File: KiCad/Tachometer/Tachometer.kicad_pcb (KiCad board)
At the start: 2 copper layers, 105 parts, among them J1 PJ301M-12, J2 PJ301M-12, J3 PJ301M-12, J4 PJ301M-12, J5 PJ301M-12, J6 PJ301M-12, J7 PJ301M-12, J8 PJ301M-12, J9 PJ301M-12, Q1 2N3904, Q10 2N3904, Q11 2N3904, Q12 2N3904, Q13 2N3904, Q14 2N3904, Q15 2N3904, Q16 2N3904, Q17 2N3904, Q18 2N3904, Q2 2N3904, Q3 2N3904, Q4 2N3904, Q5 2N3904, Q6 2N3904, Q7 2N3904, Q8 2N3904, Q9 2N3904

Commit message: all work
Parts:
- C1, C2, C3: value CP1_Small -> 470n; moved to B.Cu
- C10, C11, C12, C13, C14, C15, C5, C6, C7, C8, C9: value CP1_Small -> 100n; moved to B.Cu
- C16, C17, C18: value CP1_Small -> 22u; moved to B.Cu
- C4, H1, Q1, Q10, Q11, Q12, Q13, Q14, Q15, Q16, Q17, Q18, Q2, Q3, Q4, Q5, Q6, Q7, Q8, Q9, R1, R10, R11, R12, R13, R14, R15, R16, R17, R18, R19, R2, R20, R21, R22, R23, R24, R25, R26, R27, R28, R29, R3, R30, R31, R32, R33, R34, R35, R36, R37, R38, R39, R4, R40, R41, R42, R43, R44, R45, R5, R6, R7, R8, R9: moved to B.Cu
- D10, D11, D12: value 1N4006 -> LED; footprint Diode_THT:D_A-405_P12.70mm_Horizontal -> LED_THT:LED_D3.0mm_FlatTop
- D3, D4, D5: value LED -> 1N4006; footprint LED_THT:LED_D3.0mm_FlatTop -> Diode_THT:D_A-405_P12.70mm_Horizontal; moved to B.Cu
- moved H1 262.7 mm to (53.3, 189.2), turned to 90 degrees
- moved D3 232.2 mm to (47.0, 161.3), turned to 270 degrees
- moved D5 224.3 mm to (34.3, 161.3), turned to 270 degrees
- moved D4 187.6 mm to (59.7, 174.0), turned to 90 degrees
- moved A1 167.5 mm to (80.0, 110.5), turned to 180 degrees
- moved J3 167.5 mm to (111.8, 48.3), turned to 0 degrees
- moved D11 164.5 mm to (167.6, 20.3)
- moved D10 164.2 mm to (175.3, 29.2)
- moved J9 163.9 mm to (137.2, 39.4), turned to 0 degrees
- moved D12 156.2 mm to (175.3, 20.3)
- moved Q2 156.1 mm to (80.0, 152.4)
- moved J8 154.6 mm to (148.6, 21.6), turned to 0 degrees
- moved R23 151.4 mm to (203.2, 170.2)
- moved J5 150.5 mm to (125.7, 39.4), turned to 0 degrees
- moved Q1 148.3 mm to (80.0, 146.1), turned to 0 degrees
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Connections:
- A1 pad 30: +12V -> 12V
- C1 pad 1: GND -> 5V
- C1 pad 2: -12V -> GND
- C10 pad 1: GND -> 5V
- C10 pad 2: -12V -> GND
- C11 pad 1: +12V -> 12V
- C12 pad 1: +5V -> GND
- C12 pad 2: GND -> -12V
- C13 pad 1: GND -> 5V
- C13 pad 2: -12V -> GND
- C14 pad 1: +12V -> 12V
- C15 pad 1: +5V -> GND
- C15 pad 2: GND -> -12V
- C16 pad 1: GND -> 5V
- C16 pad 2: -12V -> GND
- C17 pad 1: +12V -> 12V
- C18 pad 1: +5V -> GND
- C18 pad 2: GND -> -12V
- C2 pad 1: +12V -> 12V
- C3 pad 1: +5V -> GND
- C3 pad 2: GND -> -12V
- C4 pad 1: GND -> 5V
- C4 pad 2: -12V -> GND
- C5 pad 1: +12V -> 12V
- C6 pad 1: +5V -> GND
- C6 pad 2: GND -> -12V
- C7 pad 1: GND -> 5V
- C7 pad 2: -12V -> GND
- C8 pad 1: +12V -> 12V
- C9 pad 1: +5V -> GND
- C9 pad 2: GND -> -12V
- D10 pad 1: +5V -> GND
- D11 pad 1: Net-(D11-Pad1) -> GND
- D11 pad 2: -12V -> Net-(D11-Pad2)
- D12 pad 1: +12V -> GND
- D3 pad 1: GND -> 12V
- D4 pad 1: GND -> Net-(D4-Pad1)
- D4 pad 2: Net-(D4-Pad2) -> -12V
- D5 pad 1: GND -> 5V
- H1 pad 1: Net-(FB2-Pad1) -> Net-(D4-Pad1)
- H1 pad 10: Net-(FB3-Pad1) -> Net-(D3-Pad2)
- H1 pad 11: Net-(FB1-Pad1) -> Net-(D5-Pad2)
- H1 pad 12: Net-(FB1-Pad1) -> Net-(D5-Pad2)
- H1 pad 2: Net-(FB2-Pad1) -> Net-(D4-Pad1)
- H1 pad 9: Net-(FB3-Pad1) -> Net-(D3-Pad2)
- Q11 pad 3: Net-(Q11-Pad3) -> Net-(J6-Pad3)
- Q14 pad 3: Net-(J8-Pad3) -> Net-(Q14-Pad3)
- Q15 pad 3: Net-(J9-Pad3) -> Net-(J8-Pad3)
- Q17 pad 3: Net-(Q17-Pad3) -> Net-(J9-Pad3)
- Q2 pad 3: Net-(J2-Pad3) -> Net-(Q2-Pad3)
- Q3 pad 3: Net-(J3-Pad3) -> Net-(J2-Pad3)
- Q4 pad 3: Net-(J4-Pad3) -> Net-(Q4-Pad3)
- Q5 pad 3: Net-(J5-Pad3) -> Net-(J3-Pad3)
- Q6 pad 3: Net-(J6-Pad3) -> Net-(Q6-Pad3)
- Q7 pad 3: Net-(Q7-Pad3) -> Net-(J4-Pad3)
- Q9 pad 3: Net-(Q9-Pad3) -> Net-(J5-Pad3)
- R1 pad 1: Net-(Q7-Pad3) -> 5V
- R1 pad 2: Net-(Q1-Pad2) -> Net-(J1-Pad3)
- R10 pad 1: +5V -> Net-(D2-Pad2)
- R10 pad 2: Net-(J4-Pad3) -> Net-(Q4-Pad2)
- R11 pad 1: +5V -> 5V
- R11 pad 2: Net-(J5-Pad3) -> Net-(J3-Pad3)
- R12 pad 1: +5V -> Net-(Q6-Pad3)
- R12 pad 2: Net-(J6-Pad3) -> Net-(Q5-Pad2)
- R13 pad 1: Net-(D1-Pad2) -> 5V
- R13 pad 2: Net-(Q7-Pad2) -> Net-(Q6-Pad3)
- R14 pad 1: Net-(D2-Pad2) -> Tr3
- R14 pad 2: Net-(Q8-Pad2) -> Net-(Q6-Pad2)
- R15 pad 1: Net-(D3-Pad2) -> Net-(D6-Pad2)
- R15 pad 2: Net-(Q9-Pad2) -> Net-(Q6-Pad2)
- R16 pad 1: Net-(D4-Pad2) -> 5V
- R16 pad 2: Net-(Q10-Pad2) -> Net-(J4-Pad3)
- R17 pad 1: Net-(D5-Pad2) -> Net-(Q8-Pad3)
- R17 pad 2: Net-(Q11-Pad2) -> Net-(Q7-Pad2)
- R18 pad 1: Net-(D6-Pad2) -> 5V
- R18 pad 2: Net-(Q12-Pad2) -> Net-(Q8-Pad3)
- R19 pad 1: +5V -> Tr4
- R19 pad 2: Net-(Q7-Pad3) -> Net-(Q8-Pad2)
- R2 pad 1: Net-(Q8-Pad3) -> Net-(Q2-Pad3)
- R2 pad 2: Net-(Q2-Pad2) -> Net-(Q1-Pad2)
- R20 pad 1: +5V -> Net-(D7-Pad2)
- R20 pad 2: Net-(Q8-Pad3) -> Net-(Q8-Pad2)
- R21 pad 1: +5V -> 5V
- R21 pad 2: Net-(Q9-Pad3) -> Net-(J5-Pad3)
- R22 pad 1: +5V -> Net-(Q10-Pad3)
- R22 pad 2: Net-(Q10-Pad3) -> Net-(Q9-Pad2)
- R23 pad 1: +5V -> 5V
- R23 pad 2: Net-(Q11-Pad3) -> Net-(Q10-Pad3)
- R24 pad 1: +5V -> Tr5
- R24 pad 2: Net-(Q12-Pad3) -> Net-(Q10-Pad2)
- R25 pad 1: Tr1 -> Net-(D8-Pad2)
- R25 pad 2: Net-(Q7-Pad2) -> Net-(Q10-Pad2)
- R26 pad 1: Tr2 -> 5V
- R26 pad 2: Net-(Q8-Pad2) -> Net-(J6-Pad3)
- R27 pad 1: Tr3 -> Net-(Q12-Pad3)
- R27 pad 2: Net-(Q9-Pad2) -> Net-(Q11-Pad2)
- R28 pad 1: Tr4 -> 5V
- R28 pad 2: Net-(Q10-Pad2) -> Net-(Q12-Pad3)
- R29 pad 1: Tr5 -> Tr6
- R29 pad 2: Net-(Q11-Pad2) -> Net-(Q12-Pad2)
- R3 pad 1: Net-(Q9-Pad3) -> 5V
- R3 pad 2: Net-(Q3-Pad2) -> Net-(Q2-Pad3)
- R30 pad 1: Tr6 -> Net-(D9-Pad2)
- R31 pad 1: Net-(Q16-Pad3) -> 5V
- R31 pad 2: Net-(Q13-Pad2) -> Net-(J7-Pad3)
- R32 pad 1: Net-(Q17-Pad3) -> Net-(Q14-Pad3)
- R32 pad 2: Net-(Q14-Pad2) -> Net-(Q13-Pad2)
- R33 pad 1: Net-(Q18-Pad3) -> 5V
- R33 pad 2: Net-(Q15-Pad2) -> Net-(Q14-Pad3)
- R34 pad 1: +5V -> Tr7
- R34 pad 2: Net-(J7-Pad3) -> Net-(Q14-Pad2)
- R35 pad 1: +5V -> Net-(D10-Pad2)
- R35 pad 2: Net-(J8-Pad3) -> Net-(Q14-Pad2)
- R36 pad 1: +5V -> 5V
- R36 pad 2: Net-(J9-Pad3) -> Net-(J8-Pad3)
- R37 pad 1: Net-(D7-Pad2) -> Net-(Q16-Pad3)
- R37 pad 2: Net-(Q16-Pad2) -> Net-(Q15-Pad2)
- R38 pad 1: Net-(D8-Pad2) -> 5V
- R38 pad 2: Net-(Q17-Pad2) -> Net-(Q16-Pad3)
- R39 pad 1: Net-(D9-Pad2) -> Tr8
- R39 pad 2: Net-(Q18-Pad2) -> Net-(Q16-Pad2)
- R4 pad 1: Net-(Q10-Pad3) -> Tr1
- R4 pad 2: Net-(Q4-Pad2) -> Net-(Q2-Pad2)
- R40 pad 1: +5V -> Net-(D11-Pad2)
- R40 pad 2: Net-(Q16-Pad3) -> Net-(Q16-Pad2)
- R41 pad 1: +5V -> 5V
- R41 pad 2: Net-(Q17-Pad3) -> Net-(J9-Pad3)
- R42 pad 1: +5V -> Net-(Q18-Pad3)
- R42 pad 2: Net-(Q18-Pad3) -> Net-(Q17-Pad2)
- R43 pad 1: Tr7 -> 5V
- R43 pad 2: Net-(Q16-Pad2) -> Net-(Q18-Pad3)
- R44 pad 1: Tr8 -> Tr9
- R44 pad 2: Net-(Q17-Pad2) -> Net-(Q18-Pad2)
- R45 pad 1: Tr9 -> Net-(D12-Pad2)
- R5 pad 1: Net-(Q11-Pad3) -> Net-(D1-Pad2)
- R5 pad 2: Net-(Q5-Pad2) -> Net-(Q2-Pad2)
- R6 pad 1: Net-(Q12-Pad3) -> 5V
- R6 pad 2: Net-(Q6-Pad2) -> Net-(J2-Pad3)
- R7 pad 1: +5V -> Net-(Q4-Pad3)
- R7 pad 2: Net-(J1-Pad3) -> Net-(Q3-Pad2)
- R8 pad 1: +5V -> 5V
- R8 pad 2: Net-(J2-Pad3) -> Net-(Q4-Pad3)
- R9 pad 1: +5V -> Tr2
- R9 pad 2: Net-(J3-Pad3) -> Net-(Q4-Pad2)

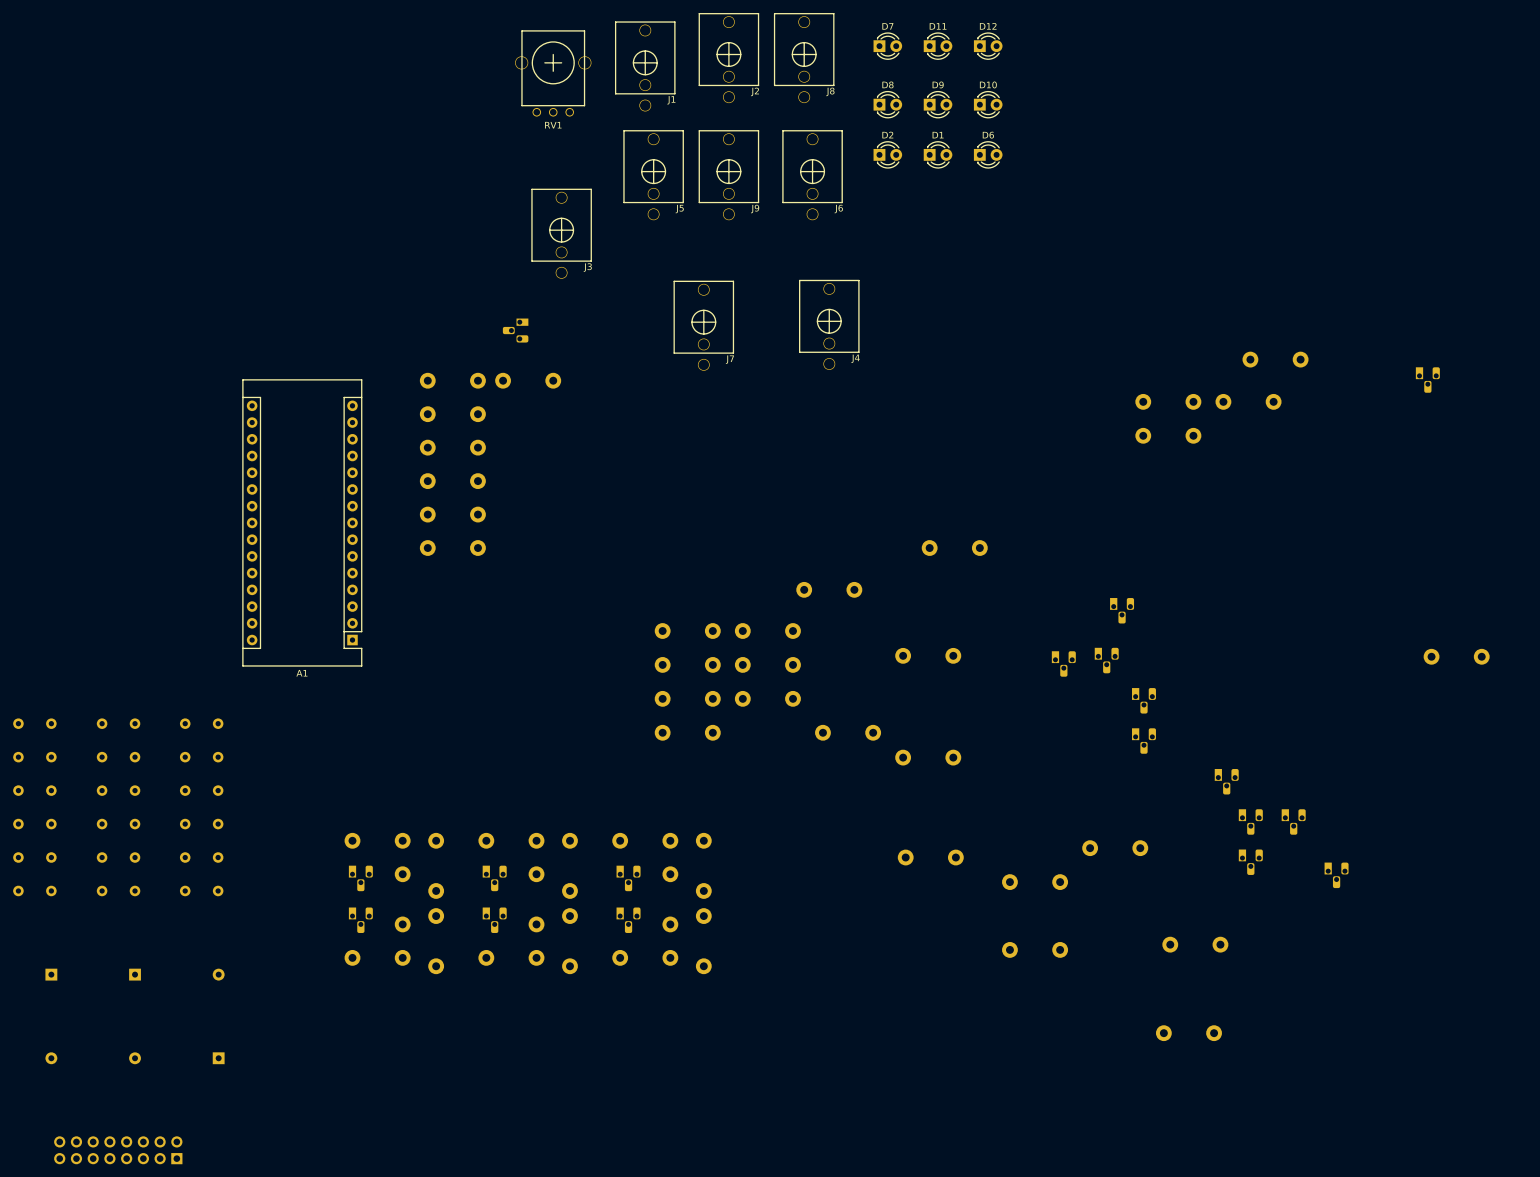
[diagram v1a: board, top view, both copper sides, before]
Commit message: added smd footprints
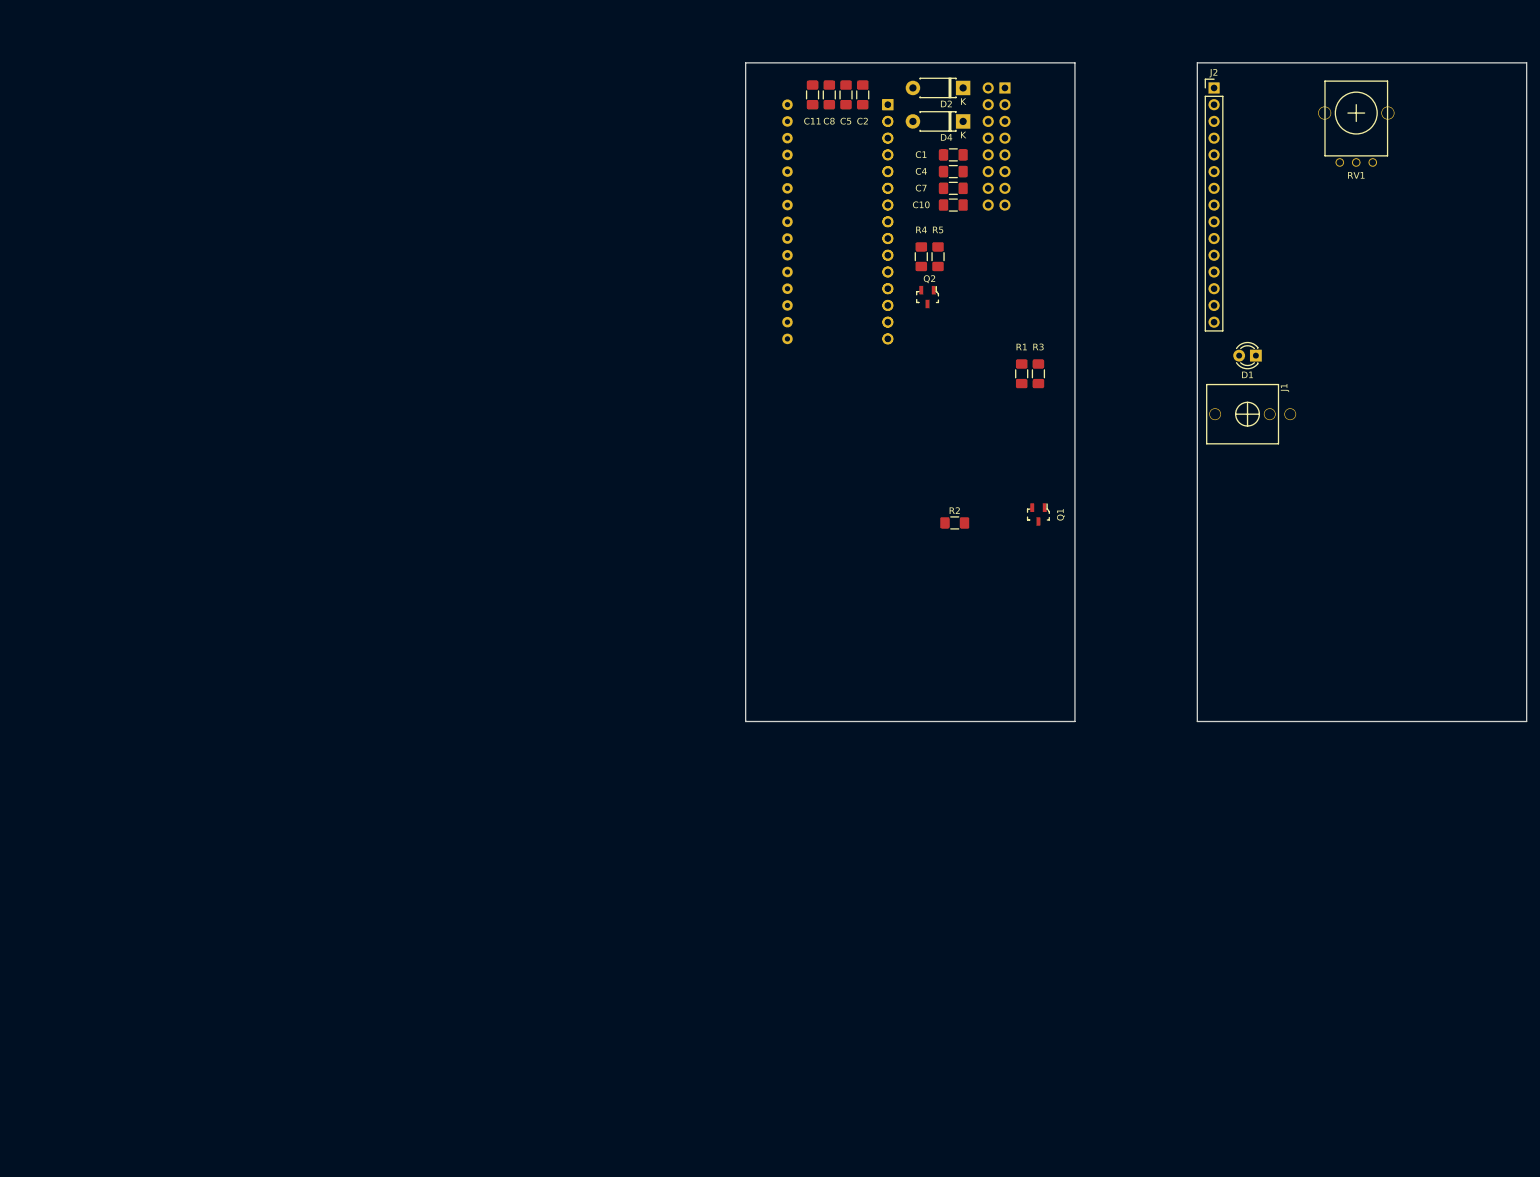
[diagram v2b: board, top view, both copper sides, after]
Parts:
- removed C12, C13, C14, C15, C6, C9: 100n, Capacitor_THT:C_Disc_D10.0mm_W2.5mm_P5.00mm
- removed C16, C17, C18: 22u, Capacitor_THT:C_Disc_D10.0mm_W2.5mm_P5.00mm
- removed C3: 470n, Capacitor_THT:C_Disc_D10.0mm_W2.5mm_P5.00mm
- removed D10, D11, D12, D6, D7, D8, D9: LED, LED_THT:LED_D3.0mm_FlatTop
- removed D3, D5: 1N4006, Diode_THT:D_A-405_P12.70mm_Horizontal
- removed J4, J5, J6, J7, J8, J9: PJ301M-12, eurorack:PJ301M-12
- removed Q10, Q11, Q12, Q13, Q14, Q15, Q16, Q17, Q18, Q3, Q4, Q5, Q6, Q7, Q8, Q9: 2N3904, Package_TO_SOT_THT:TO-92L_HandSolder
- removed R10, R11, R12, R13, R14, R15, R16, R17, R18, R19, R20, R21, R22, R23, R24, R25, R26, R27, R28, R29, R30, R31, R32, R33, R34, R35, R36, R37, R38, R39, R40, R41, R42, R43, R44, R45, R6, R7, R8, R9: R_US, Resistor_THT:R_Axial_DIN0411_L9.9mm_D3.6mm_P7.62mm_Vertical
- A1: moved to B.Cu
- C1, C2: footprint Capacitor_THT:C_Disc_D10.0mm_W2.5mm_P5.00mm -> Capacitor_SMD:C_1206_3216Metric_Pad1.42x1.75mm_HandSolder; moved to F.Cu
- C10, C11, C5, C7, C8: value 100n -> 470n; footprint Capacitor_THT:C_Disc_D10.0mm_W2.5mm_P5.00mm -> Capacitor_SMD:C_1206_3216Metric_Pad1.42x1.75mm_HandSolder; moved to F.Cu
- C4: value CP1_Small -> 470n; footprint Capacitor_THT:C_Disc_D10.0mm_W2.5mm_P5.00mm -> Capacitor_SMD:C_1206_3216Metric_Pad1.42x1.75mm_HandSolder; moved to F.Cu
- D2: value LED -> 1N4006; footprint LED_THT:LED_D3.0mm_FlatTop -> Diode_THT:D_DO-41_SOD81_P7.62mm_Horizontal
- D4: footprint Diode_THT:D_A-405_P12.70mm_Horizontal -> Diode_THT:D_DO-41_SOD81_P7.62mm_Horizontal; moved to F.Cu
- J2: value PJ301M-12 -> Conn_01x15_MountingPin; footprint eurorack:PJ301M-12 -> Connector_PinHeader_2.54mm:PinHeader_1x15_P2.54mm_Vertical
- J3: value PJ301M-12 -> Conn_01x15_MountingPin; footprint eurorack:PJ301M-12 -> Connector_PinHeader_2.54mm:PinHeader_1x15_P2.54mm_Vertical; moved to B.Cu
- Q1, Q2: footprint Package_TO_SOT_THT:TO-92L_HandSolder -> digikey-footprints:SOT-23-3; moved to F.Cu
- R1, R2, R4: value R_US -> 1k; footprint Resistor_THT:R_Axial_DIN0411_L9.9mm_D3.6mm_P7.62mm_Vertical -> Resistor_SMD:R_1206_3216Metric_Pad1.42x1.75mm_HandSolder; moved to F.Cu
- R3: value R_US -> 10k; footprint Resistor_THT:R_Axial_DIN0411_L9.9mm_D3.6mm_P7.62mm_Vertical -> Resistor_SMD:R_1206_3216Metric_Pad1.42x1.75mm_HandSolder; moved to F.Cu
- R5: value R_US -> 200; footprint Resistor_THT:R_Axial_DIN0411_L9.9mm_D3.6mm_P7.62mm_Vertical -> Resistor_SMD:R_1206_3216Metric_Pad1.42x1.75mm_HandSolder; moved to F.Cu
- moved H1 205.5 mm to (179.1, 26.7), turned to 180 degrees
- moved D4 181.7 mm to (172.7, 31.8), turned to 180 degrees
- moved C1 176.8 mm to (171.2, 36.8), turned to 0 degrees
- moved C10 169.0 mm to (171.2, 44.5), turned to 0 degrees
- moved C7 164.7 mm to (171.2, 41.9), turned to 0 degrees
- moved C2 163.8 mm to (157.5, 27.7), turned to 270 degrees
- moved C4 163.3 mm to (171.2, 39.4), turned to 0 degrees
- moved C11 154.9 mm to (149.9, 27.7), turned to 270 degrees
- moved C5 151.0 mm to (154.9, 27.7), turned to 270 degrees
- moved C8 145.7 mm to (152.4, 27.7), turned to 270 degrees
- moved R4 137.1 mm to (166.4, 52.3), turned to 270 degrees
- moved Q2 128.3 mm to (167.3, 58.4), turned to 270 degrees
- moved R5 125.8 mm to (168.9, 52.3)
- moved RV1 122.2 mm to (232.4, 30.5)
- moved R1 117.7 mm to (181.6, 70.1), turned to 270 degrees
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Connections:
- A1 pad 10: Tr6 -> Net-(A1-Pad10)
- A1 pad 11: Tr7 -> Net-(A1-Pad11)
- A1 pad 12: Tr8 -> Net-(A1-Pad12)
- A1 pad 13: Tr9 -> Net-(A1-Pad13)
- A1 pad 5: Tr1 -> Net-(A1-Pad5)
- A1 pad 6: Tr2 -> Net-(A1-Pad6)
- A1 pad 7: Tr3 -> Net-(A1-Pad7)
- A1 pad 8: Tr4 -> Net-(A1-Pad8)
- A1 pad 9: Tr5 -> Net-(A1-Pad9)
- D2 pad 1: GND -> Net-(D2-Pad1)
- D2 pad 2: Net-(D2-Pad2) -> 12V
- D4 pad 2: -12V -> 5V
- H1 pad 1: Net-(D4-Pad1) -> Net-(H1-Pad1)
- H1 pad 10: Net-(D3-Pad2) -> Net-(D2-Pad1)
- H1 pad 11: Net-(D5-Pad2) -> Net-(D4-Pad1)
- H1 pad 12: Net-(D5-Pad2) -> Net-(D4-Pad1)
- H1 pad 14: Net-(H1-Pad13) -> Net-(H1-Pad14)
- H1 pad 16: Net-(H1-Pad15) -> Net-(H1-Pad16)
- H1 pad 2: Net-(D4-Pad1) -> Net-(H1-Pad2)
- H1 pad 9: Net-(D3-Pad2) -> Net-(D2-Pad1)
- J2 pad 1: GND -> Net-(J2-Pad1)
- J2 pad 2: GND -> Net-(J2-Pad2)
- J3 pad 1: GND -> Net-(J3-Pad1)
- J3 pad 2: GND -> Net-(J3-Pad2)
- R5 pad 1: Net-(D1-Pad2) -> Tr1
- R5 pad 2: Net-(Q2-Pad2) -> Net-(D1-Pad2)
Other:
- board outline added: 118.6 x 100 mm
